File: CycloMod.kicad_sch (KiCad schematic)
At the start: 47 parts, among them J1 MICROMOD-2222, U1 10CL010YM164, U2 W25Q128JVS, U3 1.2V, U4 RP2350_60QFN, U5 MIC5504-2.5YMT, Y1 ABM8-272-T3

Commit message: incremental edits
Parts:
- removed FD1, FD2, FD3, FD4: FIDUCIALUFIDUCIAL, MicroMod-RP2040-ProcessorBoard:FIDUCIAL-MICRO, symbol MicroMod-RP2040-ProcessorBoard-eagle-import:FIDUCIALUFIDUCIAL
- removed LOGO1: SFE_LOGO_NAME_FLAME.1_INCH, MicroMod-RP2040-ProcessorBoard:SFE_LOGO_NAME_FLAME_.1, symbol MicroMod-RP2040-ProcessorBoard-eagle-import:SFE_LOGO_NAME_FLAME.1_INCH
- removed LOGO2: SFE_LOGO_FLAME.1_INCH, MicroMod-RP2040-ProcessorBoard:SFE_LOGO_FLAME_.1, symbol MicroMod-RP2040-ProcessorBoard-eagle-import:SFE_LOGO_FLAME.1_INCH
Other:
- note removed: "PIO must be contiguous for SDIO DAT pins but can fall back to SPI1"

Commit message: signals connected, still need to place decoupling
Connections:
- net GPIO4 is gone; now on net TDO: U4.7 (GPIO4)
- net GPIO5 is gone; now on net TMS: U4.8 (GPIO5)
- net CLKOUT0: now also U1.B8 (CLK10); no longer U1.A6 (IO_A6_DT11P_DATA4)
- net CLKOUT1: now also U1.A7 (CLK11); no longer U1.A4 (IO_A4_DATA7)
- net CLKOUT2: now also U1.A6 (IO_A6_DT11P_DATA4); no longer U1.B8 (CLK10)
- net CLKOUT3: now also U1.A4 (IO_A4_DATA7); no longer U1.A7 (CLK11)
- net CTS1: now also U1.A12 (IO_A12_PLL2CLKOUTP); no longer U1.B11 (IO_B11_RUP4)
- net D1: now also U1.A14 (IO_A14_DT30P_DPCLK6); no longer U1.A13 (IO_A13_VREFB7N0)
- net G0: now also U1.R14 (IO_R14_PLL4COP); no longer U1.R9 (IO_R9_DB21P)
- net G1: now also U1.R13 (IO_R13_PLL4CON); no longer U1.N8 (IO_N8_DB22P)
- net G10: now also U1.R11 (IO_R11_DPCLK3); no longer U1.R14 (IO_R14_PLL4COP)
- net G2: now also U1.P12 (IO_P12_RDN2); no longer U1.P9 (IO_P9_DB22N)
- net G3: now also U1.R12 (IO_R12_VREFB4N0); no longer U1.P10 (IO_P10)
- net G4: now also U1.N12 (IO_N12_RUP2); no longer U1.R10 (IO_R10_VREFB4N1)
- net G5: now also U1.N8 (IO_N8_DB22P); no longer U1.R11 (IO_R11_DPCLK3)
- net G6: now also U1.P9 (IO_P9_DB22N); no longer U1.N12 (IO_N12_RUP2)
- net G7: now also U1.R9 (IO_R9_DB21P); no longer U1.R12 (IO_R12_VREFB4N0)
- net G8: now also U1.P10 (IO_P10); no longer U1.P12 (IO_P12_RDN2)
- net G9: now also U1.R10 (IO_R10_VREFB4N1); no longer U1.R13 (IO_R13_PLL4CON)
- net RTS1: now also U1.B11 (IO_B11_RUP4); no longer U1.A11 (IO_A11_RDN4)
- net RX1: now also U1.A13 (IO_A13_VREFB7N0); no longer U1.B12 (IO_B12_PLL2CLKOUTN)
- net SCL: now also U1.A11 (IO_A11_RDN4), U4.13 (GPIO9); no longer U1.A14 (IO_A14_DT30P_DPCLK6), U4.10 (GPIO7)
- net SDA: now also U4.12 (GPIO8); no longer U4.9 (GPIO6)
- net TCK: now also U4.9 (GPIO6); no longer U4.14 (GPIO10)
- net TDI: now also U4.10 (GPIO7); no longer U4.15 (GPIO11)
- net TDO: no longer U4.12 (GPIO8)
- net TMS: no longer U4.13 (GPIO9)
- net TX1: now also U1.B12 (IO_B12_PLL2CLKOUTN); no longer U1.A12 (IO_A12_PLL2CLKOUTP)
- new net GPIO10: U4.14 (GPIO10)
- new net GPIO11: U4.15 (GPIO11)
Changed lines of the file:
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@@
 		)
 	)
-	(label "CLKOUT3"
+	(label "CLKOUT1"
 		(at 318.77 191.77 180)
 		(fields_autoplaced yes)
@@
 		)
 	)
-	(label "G3"
+	(label "G8"
 		(at 306.07 114.3 0)
 		(fields_autoplaced yes)
@@
 		)
 	)
-	(label "CLKOUT2"
+	(label "CLKOUT0"
 		(at 318.77 189.23 180)
 		(fields_autoplaced yes)
@@
 	)
 	(label "RX1"
-		(at 250.19 191.77 180)
-		(fields_autoplaced yes)
-		(effects
-			(font
-				(size 0.889 0.889)
-			)
-			(justify right bottom)
-		)
-	)
-	(label "G0"
+		(at 250.19 201.93 180)
+		(fields_autoplaced yes)
+		(effects
+			(font
+				(size 0.889 0.889)
+			)
+			(justify right bottom)
+		)
+	)
+	(label "G7"
 		(at 306.07 96.52 0)
 		(fields_autoplaced yes)
@@
 	)
 	(label "SCL"
-		(at 162.56 85.09 180)
+		(at 162.56 90.17 180)
 		(fields_autoplaced yes)
 		(effects
@@
 		)
 	)
-	(label "CLKOUT1"
+	(label "CLKOUT3"
 		(at 318.77 222.25 180)
 		(fields_autoplaced yes)
@@
 		)
 	)
-	(label "G6"
+	(label "G4"
 		(at 306.07 106.68 0)
 		(fields_autoplaced yes)
@@
 		)
 	)
-	(label "G5"
+	(label "G10"
 		(at 306.07 111.76 0)
 		(fields_autoplaced yes)
@@
 	)
 	(label "CTS1"
-		(at 250.19 196.85 180)
+		(at 250.19 194.31 180)
 		(fields_autoplaced yes)
 		(effects
@@
 	)
 	(label "SCL"
-		(at 250.19 207.01 180)
+		(at 250.19 199.39 180)
 		(fields_autoplaced yes)
 		(effects
@@
 		)
 	)
-	(label "GPIO5"
-		(at 162.56 80.01 180)
+	(label "GPIO11"
+		(at 162.56 95.25 180)
 		(fields_autoplaced yes)
 		(effects
@@
 		)
 	)
-	(label "G2"
+	(label "G6"
 		(at 306.07 101.6 0)
 		(fields_autoplaced yes)
@@
 		)
 	)
-	(label "G7"
+	(label "G3"
 		(at 306.07 104.14 0)
 		(fields_autoplaced yes)
@@
 		)
 	)
-	(label "CLKOUT0"
+	(label "CLKOUT2"
 		(at 318.77 219.71 180)
 		(fields_autoplaced yes)
@@
 		)
 	)
-	(label "G1"
+	(label "G5"
 		(at 306.07 99.06 0)
 		(fields_autoplaced yes)
@@
 		)
 	)
-	(label "G10"
+	(label "G0"
 		(at 306.07 116.84 0)
 		(fields_autoplaced yes)
@@
 		)
 	)
-	(label "G9"
+	(label "G1"
 		(at 306.07 119.38 0)
 		(fields_autoplaced yes)
@@
 	)
 	(label "TMS"
-		(at 162.56 90.17 180)
+		(at 162.56 80.01 180)
 		(fields_autoplaced yes)
 		(effects
@@
 	)
 	(label "TX1"
-		(at 250.19 194.31 180)
-		(fields_autoplaced yes)
-		(effects
-			(font
-				(size 0.889 0.889)
-			)
-			(justify right bottom)
-		)
-	)
-	(label "GPIO4"
-		(at 162.56 77.47 180)
+		(at 250.19 191.77 180)
+		(fields_autoplaced yes)
+		(effects
+			(font
+				(size 0.889 0.889)
+			)
+			(justify right bottom)
+		)
+	)
+	(label "GPIO10"
+		(at 162.56 92.71 180)
 		(fields_autoplaced yes)
 		(effects
@@
 	)
 	(label "TCK"
-		(at 162.56 92.71 180)
+		(at 162.56 82.55 180)
 		(fields_autoplaced yes)
 		(effects
@@
 		)
 	)
-	(label "G8"
+	(label "G2"
 		(at 306.07 109.22 0)
 		(fields_autoplaced yes)
@@
 		)
 	)
-	(label "G4"
+	(label "G9"
 		(at 306.07 121.92 0)
 		(fields_autoplaced yes)
@@
 	)
 	(label "RTS1"
-		(at 250.19 199.39 180)
+		(at 250.19 196.85 180)
 		(fields_autoplaced yes)
 		(effects
@@
 	)
 	(label "TDI"
-		(at 162.56 95.25 180)
+		(at 162.56 85.09 180)
 		(fields_autoplaced yes)
 		(effects
@@
 	)
 	(label "D1"
-		(at 250.19 201.93 180)
+		(at 250.19 207.01 180)
 		(fields_autoplaced yes)
 		(effects
@@
 	)
 	(label "SDA"
-		(at 162.56 82.55 180)
+		(at 162.56 87.63 180)
 		(fields_autoplaced yes)
 		(effects
@@
 	)
 	(label "TDO"
-		(at 162.56 87.63 180)
-		(fields_autoplaced yes)
-		(effects
+		(at 162.56 77.47 180)
+		(fields_autoplaced yes)
+		(effects

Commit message: more routing and added decoupling caps for FPGA
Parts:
- added C10, C11, C12, C13, C14, C15, C30, C31, C34, C35, C36, C37: 100n, Capacitor_SMD:C_0402_1005Metric, symbol Device:C
- added C29, C33, C9: 1u, Capacitor_SMD:C_0402_1005Metric, symbol Device:C
- added C32, C38, C8: 4.7u, Capacitor_SMD:C_0402_1005Metric, symbol Device:C
- added R2, R3: 10k, Resistor_SMD:R_0402_1005Metric, symbol Device:R
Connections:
- net +1V2: now also C32.1, C33.1, C34.1, C35.1, C36.1, C37.1
- net +2V5: now also C14.1, C15.1
- net +3V3: now also C10.1, C11.1, C12.1, C13.1, C38.1, C8.1, C9.1, R2.2, R3.1
- net CAN_RX: now also U1.F14 (IO_F14_DR17P_CRCERROR); no longer U1.F15 (IO_F15_VREFB6N1)
- net CAN_TX: now also U1.F15 (IO_F15_VREFB6N1); no longer U1.F14 (IO_F14_DR17P_CRCERROR)
- net G6: now also U1.R9 (IO_R9_DB21P); no longer U1.P9 (IO_P9_DB22N)
- net G7: now also U1.P9 (IO_P9_DB22N); no longer U1.R9 (IO_R9_DB21P)
- net G8: now also U1.R10 (IO_R10_VREFB4N1); no longer U1.P10 (IO_P10)
- net G9: now also U1.P10 (IO_P10); no longer U1.R10 (IO_R10_VREFB4N1)
- net GND: now also U1.H4 (NCE), C10.2, C11.2, C12.2, C13.2, C14.2, C15.2, C29.2, C30.2, C31.2, C32.2, C33.2, C34.2, C35.2, C36.2, C37.2, C38.2, C8.2, C9.2
- net PWM0: now also U1.C15 (IO_C15_DR2N); no longer U1.F13 (IO_F13_DR17N_INITDONE)
- net SDIO_DAT1: now also U1.R5 (IO_R5_PLL1CLKOUTN); no longer U1.P5 (IO_P5_PLL1CLKOUTP)
- net SPI_CIPO1/SDIO_DAT0: now also U1.R6 (IO_R6); no longer U1.R5 (IO_R5_PLL1CLKOUTN)
- net SPI_COPI1/SDIO_CMD: now also U1.R7 (IO_R7_DB18P); no longer U1.P7 (IO_P7_DB18N)
- net SPI_SCK1/SDIO_CLK: now also U1.P7 (IO_P7_DB18N); no longer U1.R7 (IO_R7_DB18P)
- net DONE: now reaches U1.H13 (CONF_DONE)
- net DONE: now also R2.1
- net at FB1.2, U1.B14 (VCCD_PLL2), U1.B2 (VCCD_PLL3)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: now also C29.1, C30.1, C31.1
- net nSTATUS: now reaches U1.E2 (NSTATUS)
- net nSTATUS: now also R3.2
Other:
- moved on the sheet: FB1, U1A, U1B, U1E

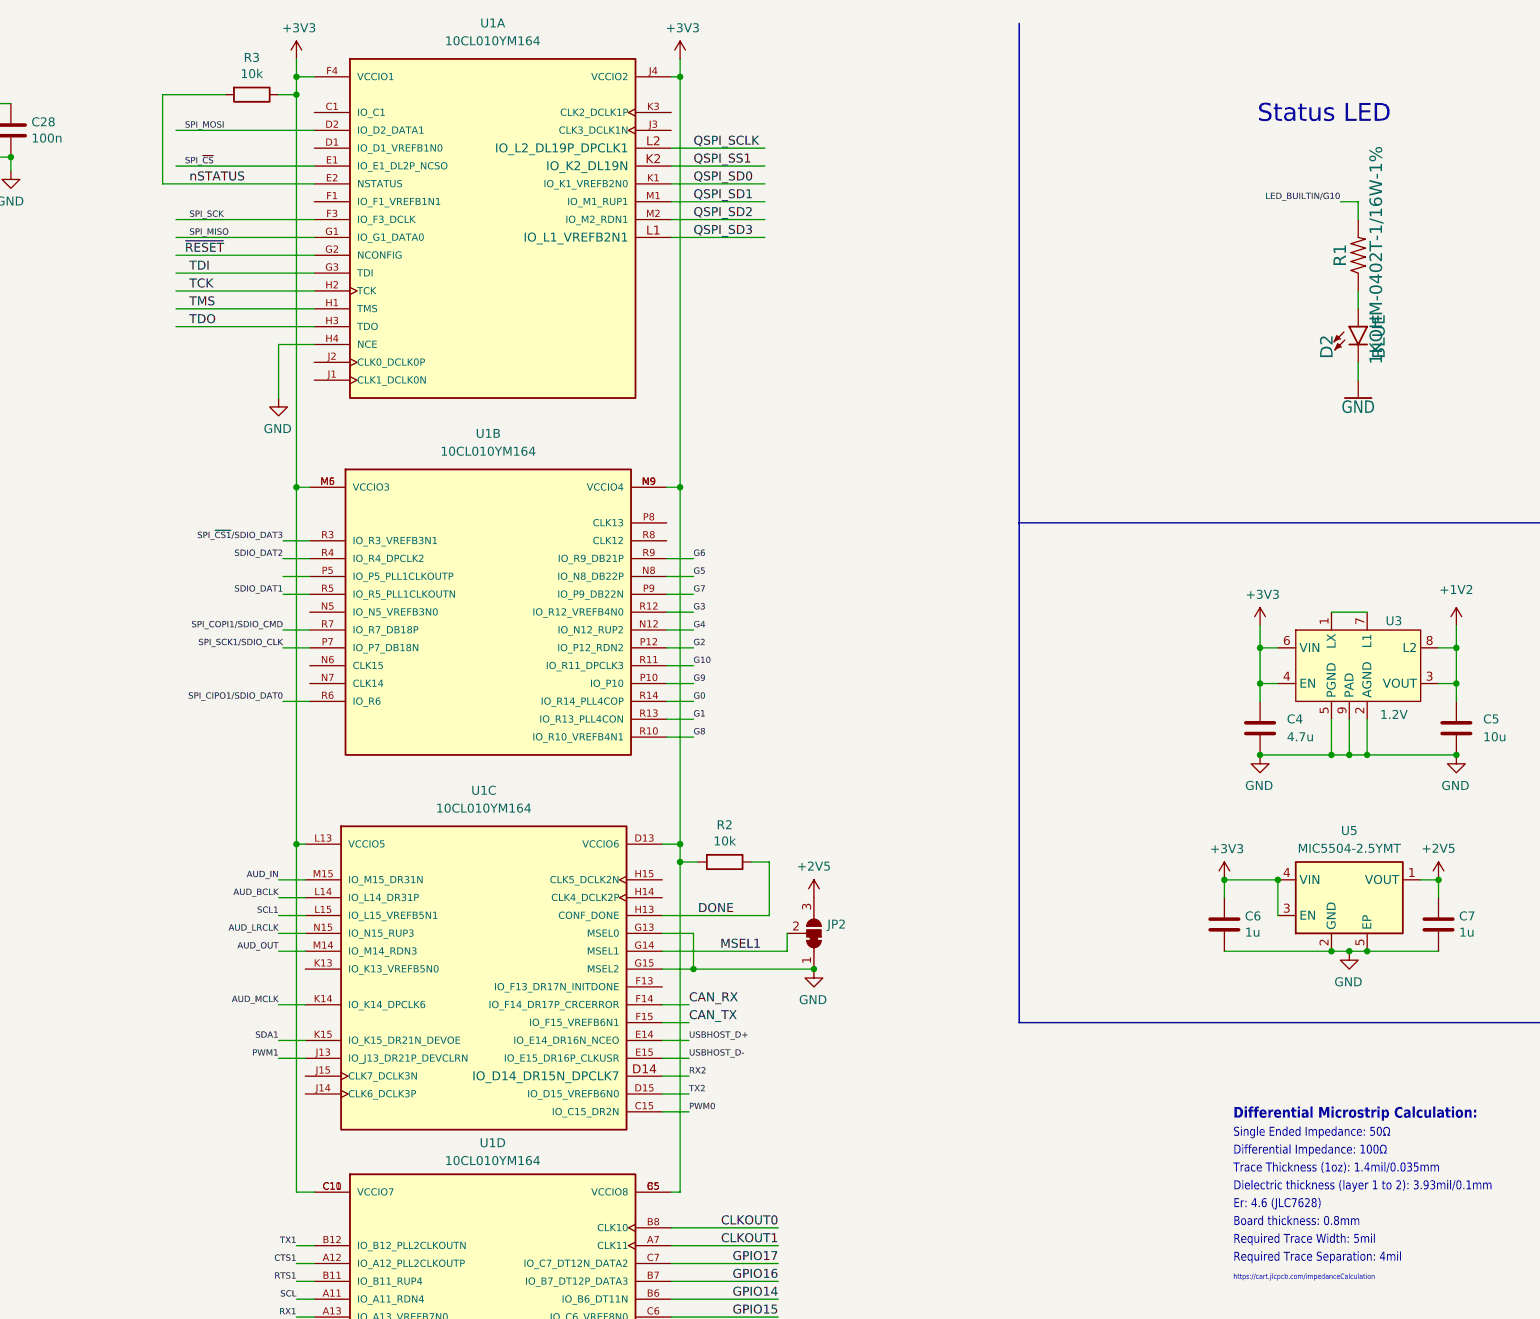
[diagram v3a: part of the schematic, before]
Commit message: more cleanup, decoupling caps in, a couple nets need connecting, more cleanup to go
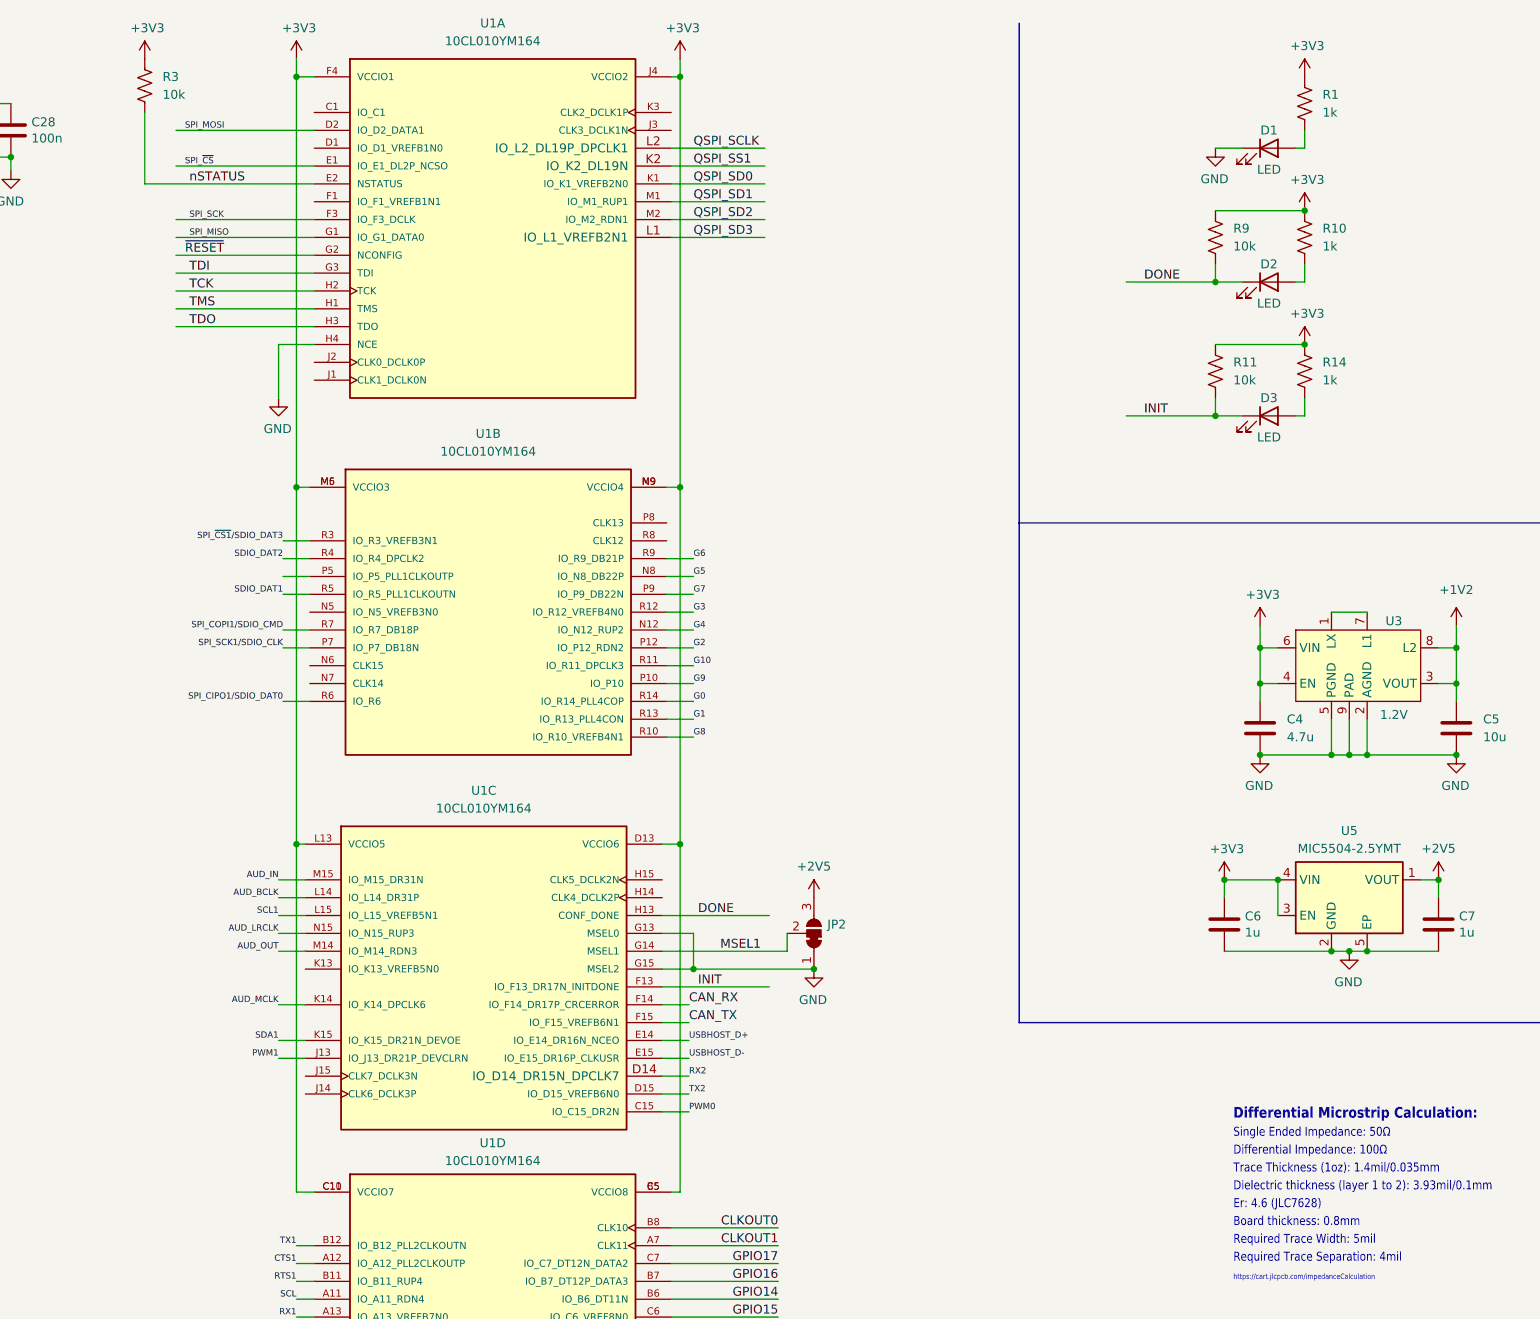
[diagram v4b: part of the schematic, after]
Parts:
- removed D2: BLUE, MicroMod-RP2040-ProcessorBoard:LED-0603, symbol MicroMod-RP2040-ProcessorBoard-eagle-import:LED-BLUE0603
- removed R1: 1KOHM-0402T-1/16W-1%, MicroMod-RP2040-ProcessorBoard:0402-TIGHT, symbol MicroMod-RP2040-ProcessorBoard-eagle-import:1KOHM-0402T-1/16W-1%
- removed R2, R3: 10k, Resistor_SMD:R_0402_1005Metric, symbol Device:R
- added D1, D2, D3: LED, LED_SMD:LED_0402_1005Metric, symbol Device:LED
- added R1, R10, R14: 1k, Resistor_SMD:R_0201_0603Metric, symbol Device:R_US
- added R11, R3, R9: 10k, Resistor_SMD:R_0201_0603Metric, symbol Device:R_US
- C1, C2: footprint Capacitor_SMD:C_0402_1005Metric -> Capacitor_SMD:C_0201_0603Metric
- C10, C11, C12, C13, C14, C15, C18, C21, C22, C23, C24, C25, C26, C27, C28, C3, C30, C31, C34, C35, C36, C37: footprint Capacitor_SMD:C_0402_1005Metric -> Capacitor_SMD:C_0201_0603Metric; LCSC (none) -> C76934; MPN (none) -> GRM033R61A104KE15D
- R12, R13, R5, R6, R7, R8: footprint Resistor_SMD:R_0402_1005Metric -> Resistor_SMD:R_0201_0603Metric
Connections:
- net +3V3: now also R1.1, R10.1, R11.1, R14.1, R3.1, R9.1
- net DONE: now also D2.1 (K), R9.2
- net GND: now also D1.1 (K)
- net nSTATUS: now also R3.2
- net INIT: now reaches U1.F13 (IO_F13_DR17N_INITDONE)
- net INIT: now also D3.1 (K), R11.2
- new net: D3.2 (A), R14.2
- new net: D2.2 (A), R10.2
- new net: D1.2 (A), R1.2
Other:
- note removed: "Status LED"

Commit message: checking in fully placed and routed.  still needs silkscreen and cleanup
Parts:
- added R2: 10k, Resistor_SMD:R_0201_0603Metric, symbol Device:R_US
- added TP1: TDI, custom:TestPoint_Pad_D0.5mm, symbol Connector:TestPoint
- added TP2: TCK, custom:TestPoint_Pad_D0.5mm, symbol Connector:TestPoint
- added TP3: TMS, custom:TestPoint_Pad_D0.5mm, symbol Connector:TestPoint
- added TP4: TDO, custom:TestPoint_Pad_D0.5mm, symbol Connector:TestPoint
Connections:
- net +3V3: now also R2.1
- net QSPI_SS1: now also R2.2
- net TCK: now also TP2.1
- net TDI: now also TP1.1
- net TDO: now also TP4.1
- net TMS: now also TP3.1

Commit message: started silkscreen cleanup, checking in prior to cardedge/outline update
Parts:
- added R4: 10k, Resistor_SMD:R_0201_0603Metric, symbol Device:R_US
- C1, C2: LCSC (none) -> C277480; MPN (none) -> CC0201JRNPO9BN150
- C10, C11, C12, C13, C14, C15, C18, C21, C22, C23, C24, C25, C26, C27, C28, C3, C30, C31, C34, C35, C36, C37: LCSC C76934 -> C76934
- C16, C17, C19, C20, C32, C38, C4, C8: LCSC (none) -> C307423; MPN (none) -> CL05A475MQ5NRNC
- C29, C33, C6, C7, C9: LCSC (none) -> C14445; MPN (none) -> CL05A105KP5NNNC
- C5: LCSC (none) -> C15525; MPN (none) -> CL05A106MQ5NUNC
- D1, D2, D3: LCSC (none) -> C6968967; MPN (none) -> IN-S42BT5B
- FB1: value FerriteBead_Small -> 120; LCSC (none) -> C85812; MPN (none) -> BLM15AG121SN1D
- FRAME1, JP2, LOGO3, LOGO4, R5, TP1, TP2, TP3, TP4: now not fitted
- J1: footprint MicroMod-RP2040-ProcessorBoard:M.2-CARD-E-22 -> custom:MicroMod_Processor; symbol MicroMod-RP2040-ProcessorBoard-eagle-import:MICROMOD-2222 -> custom:MICROMOD-2222; now not fitted
- L1: LCSC (none) -> C42411119; MPN (none) -> AOTA-B201610S3R3-101-T
- R1, R10, R14, R7, R8: LCSC (none) -> C138165; MPN (none) -> RC0201FR-071KL
- R11, R2, R3, R9: LCSC (none) -> C106225; MPN (none) -> RC0201FR-0710KL
- R12, R13: LCSC (none) -> C273268; MPN (none) -> RC0201FR-0727RL
- R6: LCSC (none) -> C295794; MPN (none) -> RC0201FR-0733RL
- U1: LCSC (none) -> C1550733; MPN (none) -> 10CL010YM164I7G
- U2: LCSC (none) -> C190862; MPN (none) -> W25Q128JVPIQ
- U3: LCSC (none) -> C6036085; MPN (none) -> XCL239B123FR-G
- U4: LCSC (none) -> C42411118; MPN (none) -> RP2350A
- U5: LCSC (none) -> C6934286; MPN (none) -> XC6233H2519R-G
- Y1: LCSC (none) -> C20625731; MPN (none) -> ABM8-272-T3
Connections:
- net +3V3: now also R4.1
- net ~{RESET}: now also R4.2
